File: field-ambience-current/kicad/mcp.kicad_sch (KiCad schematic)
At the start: 17 parts, among them SW1 Cell 1 (2u Choc V2 Hot-Swap), SW10 Modifier CLEAR (1u Choc V2 Ho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, SW2 Cell 2 (2u Choc V2 Hot-Swap), SW3 Cell 3 (2u Choc V2 Hot-Swap), SW4 Cell 4 (2u Choc V2 Hot-Swap), SW5 Cell 5 (2u Choc V2 Hot-Swap), SW6 Modifier SHIFT (1u Choc V2 Ho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, SW7 Modifier HOLD (1u Choc V2 Hot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, SW8 Modifier DRONE (1u Choc V2 Ho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, SW9 Modifier GENERATE (1u Choc V2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

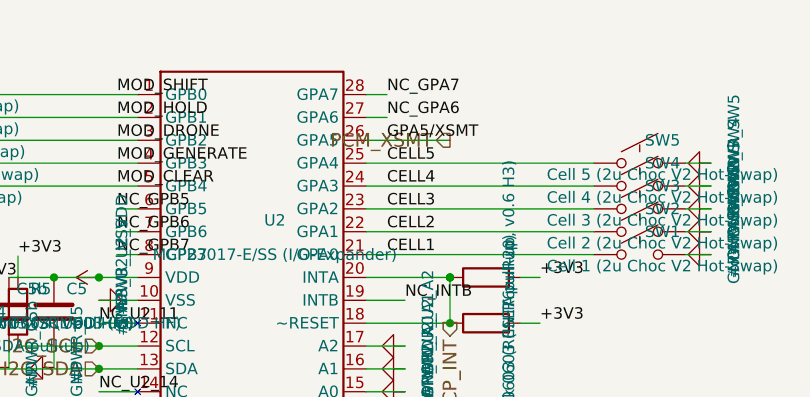
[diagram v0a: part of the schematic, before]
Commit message: v0.7-pre: Choc V2 footprint fix + Line-Out/Headphone block (J8)
Two real design improvements requested after the device evaluation.

=== 1. Switch footprint mismatch fixed (Choc V2) ===

BUG: generator referenced Button_Switch_Keyboard:SW_Hotswap_Kailh_MX_*
(MX hotswap) while BOM/SPEC specify Kailh Choc V2 throughout. MX and
Choc V2 are physically incompatible (pin spacing, height, keycap stem).
Building the MX footprint with Choc V2 sockets → parts don't fit.

FIX: footprints → Switch_Keyboard_Hotswap_Kailh:SW_Hotswap_Kailh_Choc_V1V2_*
(1.00u modifiers, 2.00u cells). Verified: 0 MX refs remain, 10 Choc refs.

LIBRARY: these are NOT in KiCad standard libs. Requires the kiswitch
keyswitch-kicad-library (PCM → Libraries → "Keyswitch Kicad Library").
Documented in SPEC §4, PCB_TODO B0, CHANGELOG. Exact footprint name must
be verified after install (B0 blocker).

=== 2. Line-Out / Headphone block (J8) — fixes the "deep character" problem ===

The 40mm onboard speakers physically cannot reproduce the 30-60Hz SubBass
the Sound Constitution is built around. Without an external output the
device's core character stays trapped in the box.

Hardware (Sheet 6 audio extended):
- J8: 3.5mm TRS jack with insertion-detect switch (PJ-320 class, C2884109)
- Passive tap from PCM5102A VOUTL/VOUTR BEFORE the PAM8403. PCM5102A output
  is ground-centered (internal charge pump) → no coupling caps needed.
- R_LO_L / R_LO_R: 22Ω series (short-circuit protection, C22962)
- Jack-detect: J8 DET switch → MCP23017 GPA6 (pull-up + IRQ enabled).
  Idle (no plug) = LOW, inserted = HIGH.

Firmware:
- New AudioPower.speakers(on) method separates speaker-amp mute from full
  system mute. Jack insert → mute ONLY the PAM8403; PCM5102A DAC + line-out
  stay live. Speaker and line-out are mutually exclusive (plug = speakers off).
- read_buttons() now reads GPA6, tracks jack state, emits {"event":"jack",
  "inserted":bool}, calls amp.speakers(not inserted) locally.
- {"set":"amp"} command now calls speake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
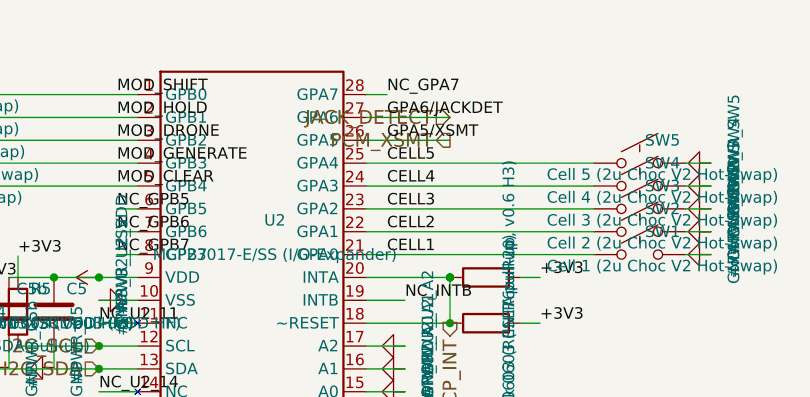
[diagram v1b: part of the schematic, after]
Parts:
- SW1, SW2, SW3, SW4, SW5: footprint Button_Switch_Keyboard:SW_Hotswap_Kailh_MX_2.00u -> Switch_Keyboard_Hotswap_Kailh:SW_Hotswap_Kailh_Choc_V1V2_2.00u
- SW10, SW6, SW7, SW8, SW9: footprint Button_Switch_Keyboard:SW_Hotswap_Kailh_MX_1.00u -> Switch_Keyboard_Hotswap_Kailh:SW_Hotswap_Kailh_Choc_V1V2_1.00u
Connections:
- net NC_GPA6 renamed JACK_DETECT
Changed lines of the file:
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@@
       (property "Value" "Cell 1 (2u Choc V2 Hot-Swap)" (at 175.62 112.53999999999999 0)
         (effects (font (size 1.27 1.27))))
-      (property "Footprint" "Button_Switch_Keyboard:SW_Hotswap_Kailh_MX_2.00u" (at 173.08 111.27 0)
+      (property "Footprint" "Switch_Keyboard_Hotswap_Kailh:SW_Hotswap_Kailh_Choc_V1V2_2.00u" (at 173.08 111.27 0)
         (effects (font (size 1.27 1.27)) hide))
       (property "Datasheet" "~" (at 173.08 111.27 0)
@@
       (property "Value" "Cell 2 (2u Choc V2 Hot-Swap)" (at 175.62 109.99999999999999 0)
         (effects (font (size 1.27 1.27))))
-      (property "Footprint" "Button_Switch_Keyboard:SW_Hotswap_Kailh_MX_2.00u" (at 173.08 108.72999999999999 0)
+      (property "Footprint" "Switch_Keyboard_Hotswap_Kailh:SW_Hotswap_Kailh_Choc_V1V2_2.00u" (at 173.08 108.72999999999999 0)
         (effects (font (size 1.27 1.27)) hide))
       (property "Datasheet" "~" (at 173.08 108.72999999999999 0)
@@
       (property "Value" "Cell 3 (2u Choc V2 Hot-Swap)" (at 175.62 107.46 0)
         (effects (font (size 1.27 1.27))))
-      (property "Footprint" "Button_Switch_Keyboard:SW_Hotswap_Kailh_MX_2.00u" (at 173.08 106.19 0)
+      (property "Footprint" "Switch_Keyboard_Hotswap_Kailh:SW_Hotswap_Kailh_Choc_V1V2_2.00u" (at 173.08 106.19 0)
         (effects (font (size 1.27 1.27)) hide))
       (property "Datasheet" "~" (at 173.08 106.19 0)
@@
       (property "Value" "Cell 4 (2u Choc V2 Hot-Swap)" (at 175.62 104.91999999999999 0)
         (effects (font (size 1.27 1.27))))
-      (property "Footprint" "Button_Switch_Keyboard:SW_Hotswap_Kailh_MX_2.00u" (at 173.08 103.64999999999999 0)
+      (property "Footprint" "Switch_Keyboard_Hotswap_Kailh:SW_Hotswap_Kailh_Choc_V1V2_2.00u" (at 173.08 103.64999999999999 0)
         (effects (font (size 1.27 1.27)) hide))
       (property "Datasheet" "~" (at 173.08 103.64999999999999 0)
@@
       (property "Value" "Cell 5 (2u Choc V2 Hot-Swap)" (at 175.62 102.38 0)
         (effects (font (size 1.27 1.27))))
-      (property "Footprint" "Button_Switch_Keyboard:SW_Hotswap_Kailh_MX_2.00u" (at 173.08 101.11 0)
+      (property "Footprint" "Switch_Keyboard_Hotswap_Kailh:SW_Hotswap_Kailh_Choc_V1V2_2.00u" (at 173.08 101.11 0)
         (effects (font (size 1.27 1.27)) hide))
       (property "Datasheet" "~" (at 173.08 101.11 0)
@@
       (property "Value" "Modifier SHIFT (1u Choc V2 Hot-Swap)" (at 87.46000000000001 94.75999999999999 0)
         (effects (font (size 1.27 1.27))))
-      (property "Footprint" "Button_Switch_Keyboard:SW_Hotswap_Kailh_MX_1.00u" (at 84.92 93.49 0)
+      (property "Footprint" "Switch_Keyboard_Hotswap_Kailh:SW_Hotswap_Kailh_Choc_V1V2_1.00u" (at 84.92 93.49 0)
         (effects (font (size 1.27 1.27)) hide))
       (property "Datasheet" "~" (at 84.92 93.49 0)
@@
       (property "Value" "Modifier HOLD (1u Choc V2 Hot-Swap)" (at 87.46000000000001 97.3 0)
         (effects (font (size 1.27 1.27))))
-      (property "Footprint" "Button_Switch_Keyboard:SW_Hotswap_Kailh_MX_1.00u" (at 84.92 96.03 0)
+      (property "Footprint" "Switch_Keyboard_Hotswap_Kailh:SW_Hotswap_Kailh_Choc_V1V2_1.00u" (at 84.92 96.03 0)
         (effects (font (size 1.27 1.27)) hide))
       (property "Datasheet" "~" (at 84.92 96.03 0)
@@
       (property "Value" "Modifier DRONE (1u Choc V2 Hot-Swap)" (at 87.46000000000001 99.83999999999999 0)
         (effects (font (size 1.27 1.27))))
-      (property "Footprint" "Button_Switch_Keyboard:SW_Hotswap_Kailh_MX_1.00u" (at 84.92 98.57 0)
+      (property "Footprint" "Switch_Keyboard_Hotswap_Kailh:SW_Hotswap_Kailh_Choc_V1V2_1.00u" (at 84.92 98.57 0)
         (effects (font (size 1.27 1.27)) hide))
       (property "Datasheet" "~" (at 84.92 98.57 0)
@@
       (property "Value" "Modifier GENERATE (1u Choc V2 Hot-Swap)" (at 87.46000000000001 102.38 0)
         (effects (font (size 1.27 1.27))))
-      (property "Footprint" "Button_Switch_Keyboard:SW_Hotswap_Kailh_MX_1.00u" (at 84.92 101.11 0)
+      (property "Footprint" "Switch_Keyboard_Hotswap_Kailh:SW_Hotswap_Kailh_Choc_V1V2_1.00u" (at 84.92 101.11 0)
         (effects (font (size 1.27 1.27)) hide))
       (property "Datasheet" "~" (at 84.92 101.11 0)
@@
       (property "Value" "Modifier CLEAR (1u Choc V2 Hot-Swap)" (at 87.46000000000001 104.91999999999999 0)
         (effects (font (size 1.27 1.27))))
-      (property "Footprint" "Button_Switch_Keyboard:SW_Hotswap_Kailh_MX_1.00u" (at 84.92 103.64999999999999 0)
+      (property "Footprint" "Switch_Keyboard_Hotswap_Kailh:SW_Hotswap_Kailh_Choc_V1V2_1.00u" (at 84.92 103.64999999999999 0)
         (effects (font (size 1.27 1.27)) hide))
       (property "Datasheet" "~" (at 84.92 103.64999999999999 0)
@@
     (stroke (width 0) (type default))
 )
-  (wire (pts (xy 142.7 96.03) (xy 145 96.03))
+  (wire (pts (xy 142.7 96.03) (xy 152 96.03))
     (stroke (width 0) (type default))
 )
@@
     (effects (font (size 1.27 1.27)) (justify left bottom))
 )
-  (label "NC_GPA6" (at 145 96.03 0) (fields_autoplaced)
+  (label "GPA6/JACKDET" (at 145 96.03 0) (fields_autoplaced)
     (effects (font (size 1.27 1.27)) (justify left bottom))
 )
@@
     (effects (font (size 1.524 1.524)) (justify right))
 )
+  (hierarchical_label "JACK_DETECT" (shape input) (at 152 96.03 180)
+    (effects (font (size 1.524 1.524)) (justify right))
+)

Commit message: fix(bom): make entire BOM correctly JLC-orderable — 7 real part errors fixed
Verified every LCSC number against jlcsearch for existence, stock, AND that
it resolves to the intended value/package. Found 7 parts that would have
built WRONG or were unorderable:

CRITICAL value/package errors (LCSC pointed at the wrong part):
- R_VOL_L/R: C25092 = 22ohm 0402  -> C4184  (real 20k 0603, Basic).
  Was wrong value AND footprint; would have wrecked the PAM8403 input gain.
- R_LO_L/R:  C22962 = 220ohm       -> C23345 (real 22ohm 0603, Basic).
- R_BCK/LRCK/DOUT: C23138 = 330ohm -> C23140 (real 33ohm 0603, Basic).

Unorderable -> assigned real in-stock parts:
- J8 jack:  C2884109 (nonexistent) -> C431535 (PJ-320D SMD).
- C_BULK:   placeholder            -> C46550395 (1000uF 16V SMD D10x10.5).
- LED1:     no LCSC                -> C965818 (white 0805).
- R1:       C22548 Extended        -> C21190 Basic (prior commit).

Also aligned all MPN text to the actual LCSC part (Yageo text vs Uni Royal/
Samsung parts JLC ships) so the BOM is internally consistent.

Re-verified: 25 distinct LCSC, all in stock, ZERO value/package mismatches,
14 Basic / 11 Extended. SPEC §4 stale refs (C_BULK/J8/R_LO) updated.
MEINE_TODO Abschnitt 0 rewritten with the full orderability result.

Self-supply parts (Pico, OLED, speakers, Choc sockets, EC11, headers) keep
no LCSC by design — JLC cannot assemble those.

https://claude.ai/code/session_01K5kLTFpDCCoYwx2dq6RkAv
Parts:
- C5b: MPN CC0603KRX7R9BB103 -> 0603B103K500NT
- R20, R6: MPN RC0603FR-0710KL -> 0603WAF1002T5E
- R4, R5: MPN RC0603FR-074K7L -> 0603WAF4701T5E
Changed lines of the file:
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@@
       (property "Datasheet" "~" (at 103 117.62 0)
         (effects (font (size 1.27 1.27)) hide))
-      (property "MPN" "CC0603KRX7R9BB103" (at 105.54 121.43 0)
+      (property "MPN" "0603B103K500NT" (at 105.54 121.43 0)
         (effects (font (size 1.27 1.27)) hide))
       (property "LCSC" "C57112" (at 105.54 122.7 0)
@@
       (property "Datasheet" "~" (at 104 117.61999999999999 0)
         (effects (font (size 1.27 1.27)) hide))
-      (property "MPN" "RC0603FR-074K7L" (at 106.54 121.42999999999999 0)
+      (property "MPN" "0603WAF4701T5E" (at 106.54 121.42999999999999 0)
         (effects (font (size 1.27 1.27)) hide))
       (property "LCSC" "C23162" (at 106.54 122.69999999999999 0)
@@
       (property "Datasheet" "~" (at 99 120.16 0)
         (effects (font (size 1.27 1.27)) hide))
-      (property "MPN" "RC0603FR-074K7L" (at 101.54 123.97 0)
+      (property "MPN" "0603WAF4701T5E" (at 101.54 123.97 0)
         (effects (font (size 1.27 1.27)) hide))
       (property "LCSC" "C23162" (at 101.54 125.24 0)
@@
       (property "Datasheet" "~" (at 156 118.88999999999999 0)
         (effects (font (size 1.27 1.27)) hide))
-      (property "MPN" "RC0603FR-0710KL" (at 158.54 122.69999999999999 0)
+      (property "MPN" "0603WAF1002T5E" (at 158.54 122.69999999999999 0)
         (effects (font (size 1.27 1.27)) hide))
       (property "LCSC" "C25804" (at 158.54 123.96999999999998 0)
@@
       (property "Datasheet" "~" (at 156 113.81 0)
         (effects (font (size 1.27 1.27)) hide))
-      (property "MPN" "RC0603FR-0710KL" (at 158.54 117.62 0)
+      (property "MPN" "0603WAF1002T5E" (at 158.54 117.62 0)
         (effects (font (size 1.27 1.27)) hide))
       (property "LCSC" "C25804" (at 158.54 118.89 0)
